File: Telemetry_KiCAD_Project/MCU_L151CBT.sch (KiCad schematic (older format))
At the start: 15 parts

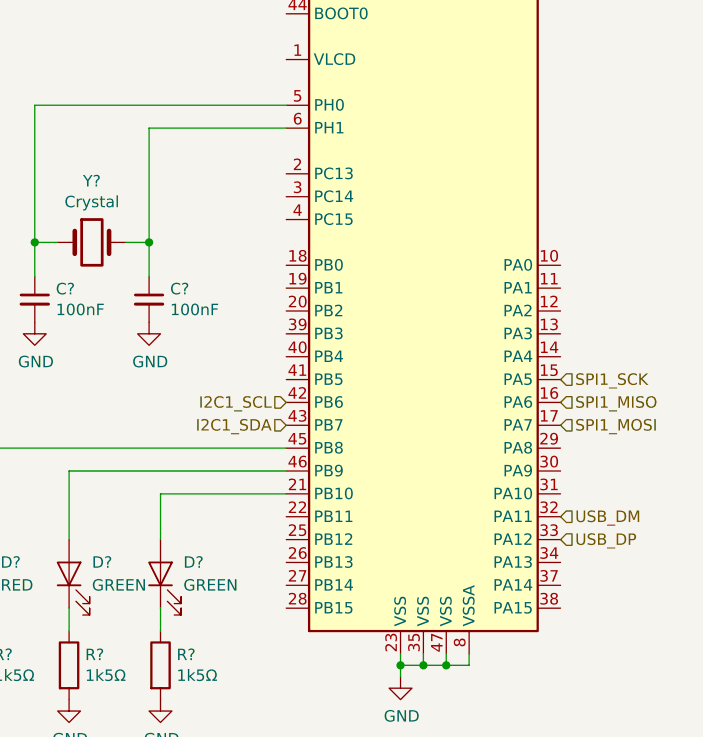
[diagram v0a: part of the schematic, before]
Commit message: Included Amplifier, New Transceivers, Duplexer, and 37 Pin DSUB
Still want to replace the microcontroller, will happen in next commit
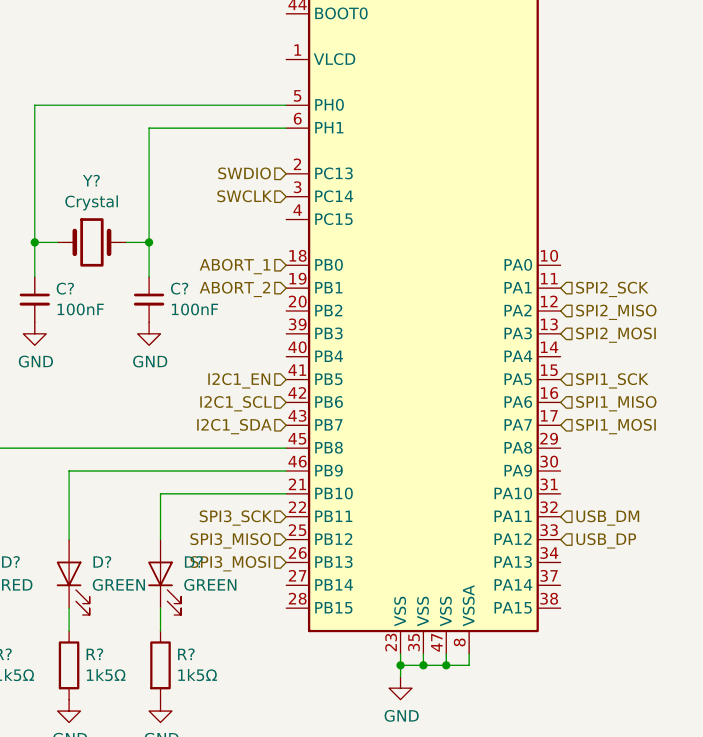
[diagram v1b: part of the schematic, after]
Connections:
- net SPI2_SCK: now reaches U?.11 (PA1)
- net SPI2_MISO: now reaches U?.12 (PA2)
- net SPI2_MOSI: now reaches U?.13 (PA3)
- net ABORT_1: now reaches U?.18 (PB0)
- net ABORT_2: now reaches U?.19 (PB1)
- net SWDIO: now reaches U?.2 (PC13)
- net SPI3_SCK: now reaches U?.22 (PB11)
- net SPI3_MISO: now reaches U?.25 (PB12)
- net SPI3_MOSI: now reaches U?.26 (PB13)
- net SWCLK: now reaches U?.3 (PC14)
- net I2C1_EN: now reaches U?.41 (PB5)
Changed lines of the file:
@@
 EESchema Schematic File Version 4
-EELAYER 30 0
+LIBS:Telemetry_KiCAD_Project-cache
+EELAYER 29 0
 EELAYER END
 $Descr A4 11693 8268
 encoding utf-8
-Sheet 2 3
+Sheet 2 7
 Title "STM32L151CBT Schematic"
 Date "2021-10-01"
@@
 Wire Notes Line
 	3400 800  950  800
+Text HLabel 9050 3750 2    50   Input ~ 0
+SPI2_SCK
+Text HLabel 9050 3850 2    50   Input ~ 0
+SPI2_MISO
+Text HLabel 9050 3950 2    50   Input ~ 0
+SPI2_MOSI
+Text HLabel 7850 4750 0    50   Input ~ 0
+SPI3_SCK
+Text HLabel 7850 4850 0    50   Input ~ 0
+SPI3_MISO
+Text HLabel 7850 4950 0    50   Input ~ 0
+SPI3_MOSI
+Text HLabel 7850 4150 0    50   Input ~ 0
+I2C1_EN
+Text HLabel 7850 3650 0    50   Input ~ 0
+ABORT_1
+Text HLabel 7850 3750 0    50   Input ~ 0
+ABORT_2
+Text HLabel 7850 3250 0    50   Input ~ 0
+SWDIO
+Text HLabel 7850 3350 0    50   Input ~ 0
+SWCLK
 $EndSCHEMATC
